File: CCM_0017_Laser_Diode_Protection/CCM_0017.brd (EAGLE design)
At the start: 32.4 x 9.5 mm, 6 parts, among them T1 FMMT4901, X1 22-23-2021, X2 22-23-2021

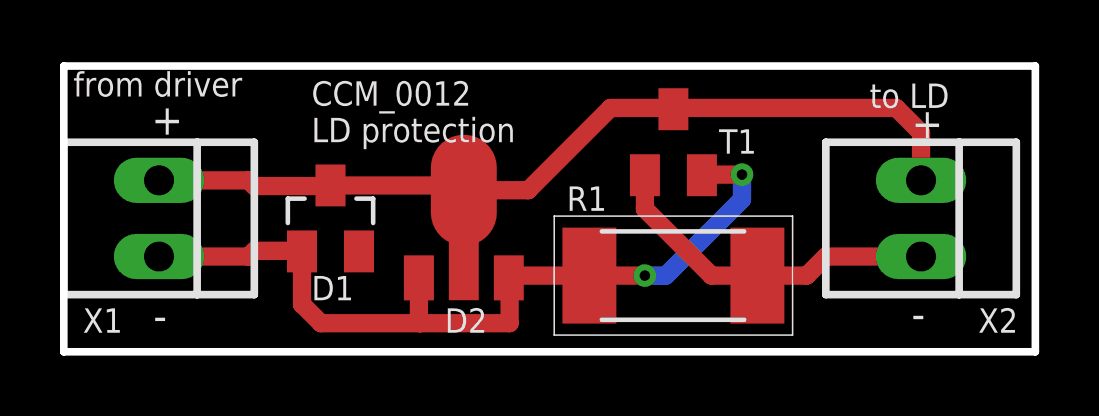
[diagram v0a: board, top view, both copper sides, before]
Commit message: Shutter driver added.
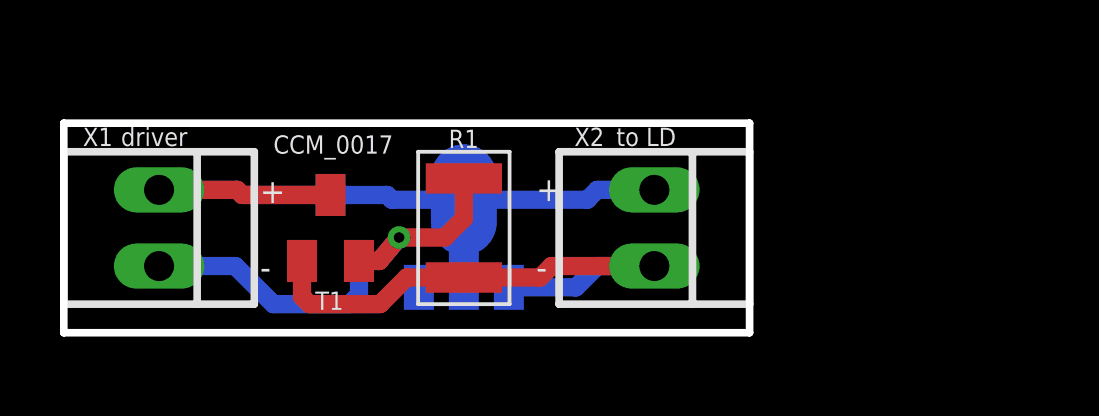
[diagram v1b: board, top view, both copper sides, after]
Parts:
- R1: device noah:2512 -> noah:1210
- moved T1 11.8 mm to (8.89, 4.13)
- moved X2 8.90 mm to (19.7, 4.13)
- moved R1 7.16 mm to (13.3, 4.13), turned to 90 degrees
- moved D1 0.32 mm to (8.89, 4.13), flipped to the bottom
- moved D2 0.32 mm to (13.3, 4.13), flipped to the bottom
- moved X1 0.32 mm to (3.17, 4.13)
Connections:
- net N$4: now also D2.1, D2.3
- net N$5: no longer D2.1, D2.3
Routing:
- net N$5: track 27.9 -> 15.6 mm, vias 2 -> 1
- net N$4: track 11.5 -> 18.7 mm
- net N$7: track 28.7 -> 22.6 mm
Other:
- board size 32.4 x 9.5 mm -> 22.9 x 7 mm
- board text added: "CCM_0017"
- board text added: "driver"
- board text removed: "CCM_0012 LD protection"
- board text removed: "from driver"
